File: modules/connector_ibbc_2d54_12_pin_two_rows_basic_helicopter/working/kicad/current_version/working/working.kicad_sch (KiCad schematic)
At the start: 2 parts, among them J1 hi16p, J2 hi16p

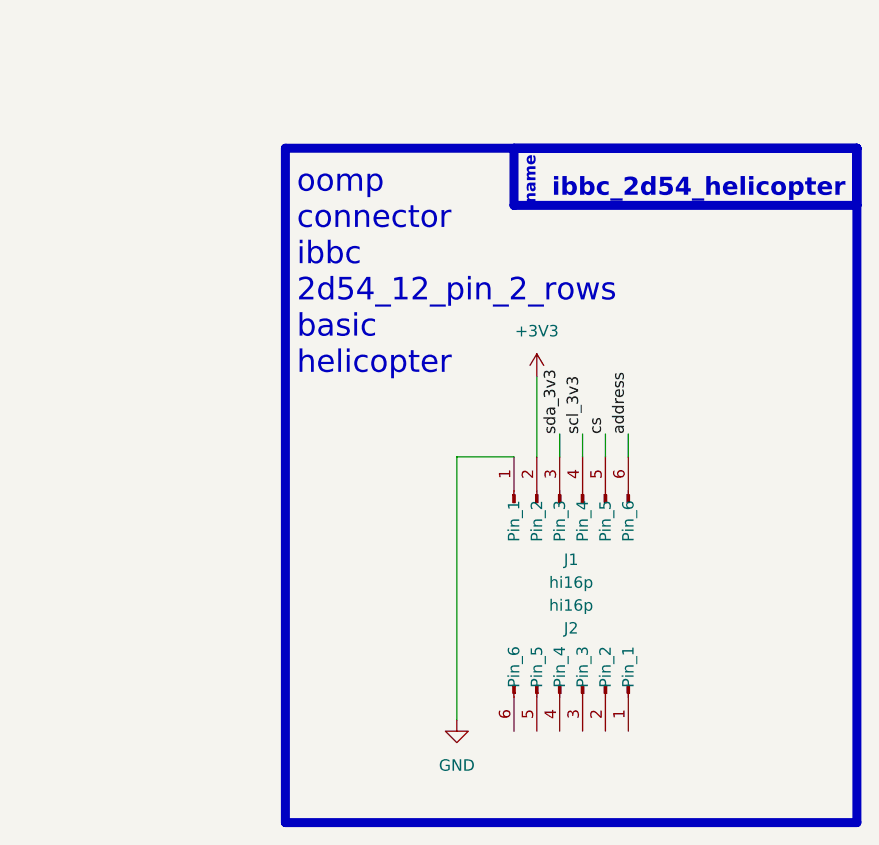
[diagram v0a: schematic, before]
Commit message: fixed formatting to be more consistent
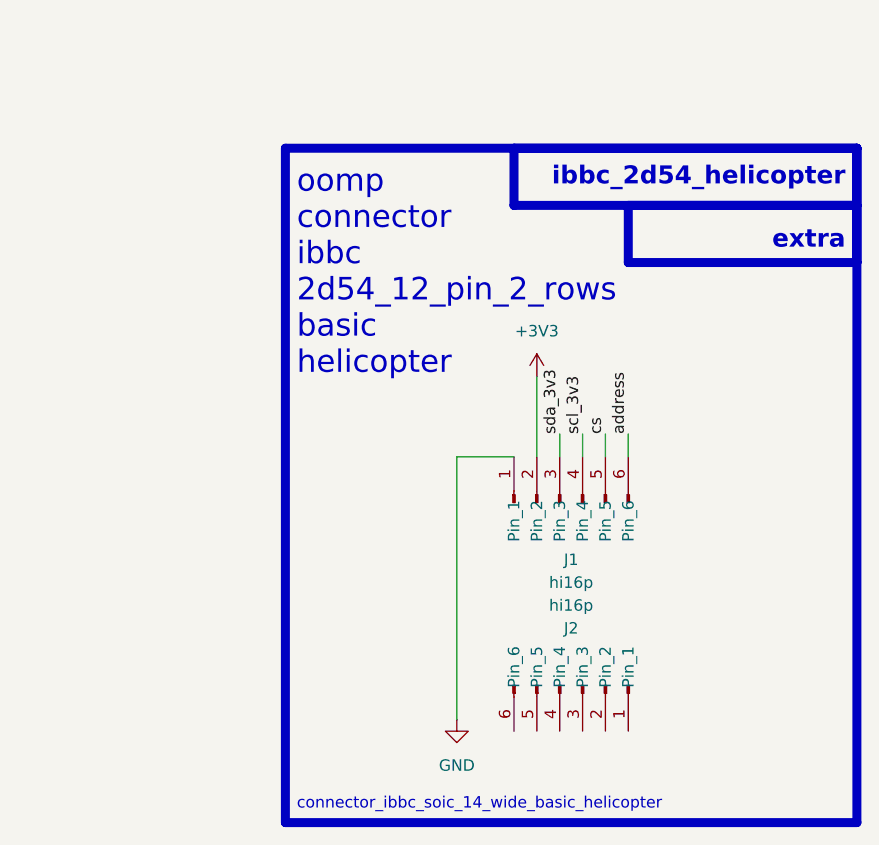
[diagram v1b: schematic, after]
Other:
- note added: "connector_ibbc_soic_14_wide_basic_helicopter"
- note added: "extra"
- note removed: "name"
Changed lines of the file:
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@@
   (rectangle (start 129.54 46.99) (end 167.64 53.34)
     (stroke (width 1) (type default))
-    (fill (type color) (color 0 0 0 0))
+    (fill (type none))
   )
-  (text "ibbc_2d54_helicopter\n	" (at 166.37 55.88 0)
-    (effects (font (size 2 2) (thickness 0.8) bold (color 255 255 255 1)) (justify right bottom))
+  (rectangle (start 142.24 53.34) (end 167.64 59.69)
+    (stroke (width 1) (type default))
+    (fill (type none))
   )
-  (text "name" (at 132.08 53.34 90)
-    (effects (font (size 1.27 1.27) (thickness 0.254) bold (color 255 255 255 1)) (justify left bottom))
+  (text "ibbc_2d54_helicopter\n	" (at 166.37 54.61 0)
+    (effects (font (size 2 2) (thickness 0.8) bold) (justify right bottom))
   )
   (text "oomp\nconnector\nibbc\n2d54_12_pin_2_rows\nbasic\nhelicopter"
@@
     (effects (font (size 2.5 2.5)) (justify left bottom))
   )
+  (text "extra" (at 166.37 58.42 0)
+    (effects (font (size 2 2) (thickness 0.8) bold) (justify right bottom))
+  )
+  (text "connector_ibbc_soic_14_wide_basic_helicopter" (at 105.41 120.65 0)
+    (effects (font (size 1.27 1.27)) (justify left bottom))
+  )
   (label "address" (at 142.24 78.74 90) (fields_autoplaced)

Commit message: schematic formatting
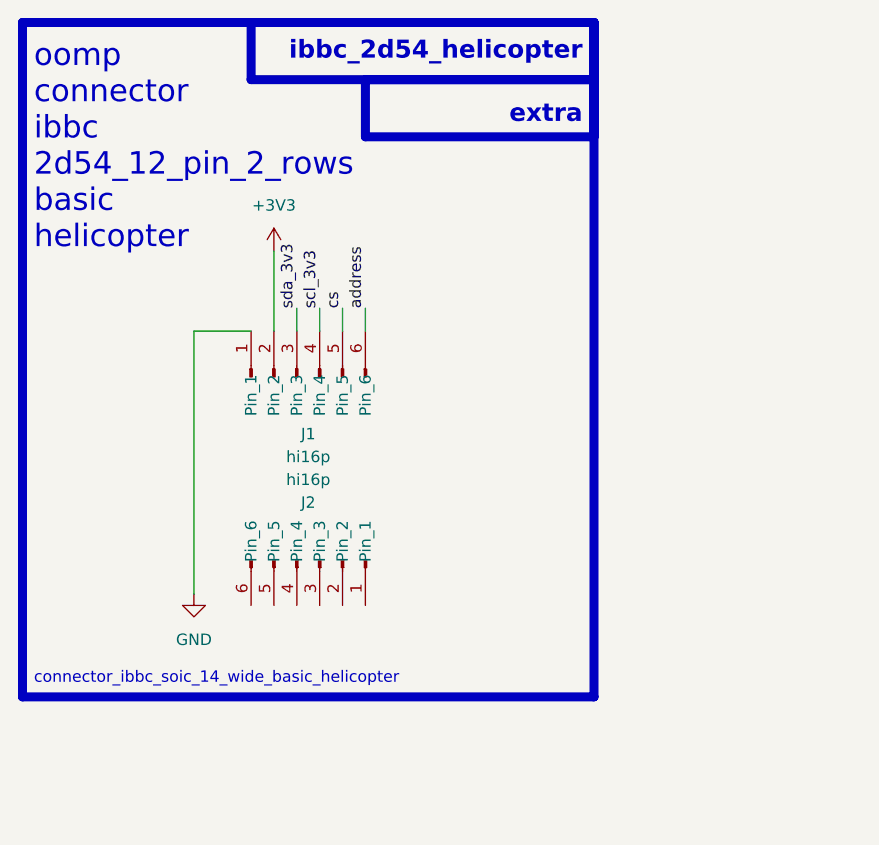
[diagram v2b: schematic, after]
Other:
- moved on the sheet: J1, J2
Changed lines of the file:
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@@
 (kicad_sch (version 20230121) (generator eeschema)
-  (paper "A4")
-  (wire (pts (xy 137.16 78.74) (xy 137.16 81.28))
+  (paper "A5")
+  (wire (pts (xy 107.95 64.77) (xy 107.95 67.31))
     (stroke (width 0) (type default))
   )
-  (wire (pts (xy 123.19 81.28) (xy 123.19 110.49))
+  (wire (pts (xy 93.98 67.31) (xy 93.98 96.52))
     (stroke (width 0) (type default))
   )
-  (wire (pts (xy 134.62 78.74) (xy 134.62 81.28))
+  (wire (pts (xy 105.41 64.77) (xy 105.41 67.31))
     (stroke (width 0) (type default))
   )
-  (wire (pts (xy 132.08 72.39) (xy 132.08 81.28))
+  (wire (pts (xy 102.87 58.42) (xy 102.87 67.31))
     (stroke (width 0) (type default))
   )
-  (wire (pts (xy 142.24 78.74) (xy 142.24 81.28))
+  (wire (pts (xy 113.03 64.77) (xy 113.03 67.31))
     (stroke (width 0) (type default))
   )
-  (wire (pts (xy 129.54 81.28) (xy 123.19 81.28))
+  (wire (pts (xy 100.33 67.31) (xy 93.98 67.31))
     (stroke (width 0) (type default))
   )
-  (wire (pts (xy 139.7 78.74) (xy 139.7 81.28))
+  (wire (pts (xy 110.49 64.77) (xy 110.49 67.31))
     (stroke (width 0) (type default))
   )
-  (rectangle (start 104.14 46.99) (end 167.64 121.92)
+  (rectangle (start 74.93 33.02) (end 138.43 107.95)
     (stroke (width 1) (type default))
     (fill (type none))
   )
-  (rectangle (start 129.54 46.99) (end 167.64 53.34)
+  (rectangle (start 100.33 33.02) (end 138.43 39.37)
     (stroke (width 1) (type default))
     (fill (type none))
   )
-  (rectangle (start 142.24 53.34) (end 167.64 59.69)
+  (rectangle (start 113.03 39.37) (end 138.43 45.72)
     (stroke (width 1) (type default))
     (fill (type none))
   )
-  (text "ibbc_2d54_helicopter\n	" (at 166.37 54.61 0)
+  (text "ibbc_2d54_helicopter\n	" (at 137.16 40.64 0)
     (effects (font (size 2 2) (thickness 0.8) bold) (justify right bottom))
   )
   (text "oomp\nconnector\nibbc\n2d54_12_pin_2_rows\nbasic\nhelicopter"
-    (at 105.41 72.39 0)
+    (at 76.2 58.42 0)
     (effects (font (size 2.5 2.5)) (justify left bottom))
   )
-  (text "extra" (at 166.37 58.42 0)
+  (text "extra" (at 137.16 44.45 0)
     (effects (font (size 2 2) (thickness 0.8) bold) (justify right bottom))
   )
-  (text "connector_ibbc_soic_14_wide_basic_helicopter" (at 105.41 120.65 0)
+  (text "connector_ibbc_soic_14_wide_basic_helicopter" (at 76.2 106.68 0)
     (effects (font (size 1.27 1.27)) (justify left bottom))
   )
-  (label "address" (at 142.24 78.74 90) (fields_autoplaced)
+  (label "address" (at 113.03 64.77 90) (fields_autoplaced)
     (effects (font (size 1.27 1.27)) (justify left bottom))
   )
-  (label "cs" (at 139.7 78.74 90) (fields_autoplaced)
+  (label "cs" (at 110.49 64.77 90) (fields_autoplaced)
     (effects (font (size 1.27 1.27)) (justify left bottom))
   )
-  (label "scl_3v3" (at 137.16 78.74 90) (fields_autoplaced)
+  (label "scl_3v3" (at 107.95 64.77 90) (fields_autoplaced)
     (effects (font (size 1.27 1.27)) (justify left bottom))
   )
-  (label "sda_3v3" (at 134.62 78.74 90) (fields_autoplaced)
+  (label "sda_3v3" (at 105.41 64.77 90) (fields_autoplaced)
     (effects (font (size 1.27 1.27)) (justify left bottom))
   )
-  (symbol (lib_id "oomlout_oomp_part_symbols:hi16p_electronic_header_2d54_mm_6_pin") (at 134.62 86.36 90) (unit 1)
+  (symbol (lib_id "oomlout_oomp_part_symbols:hi16p_electronic_header_2d54_mm_6_pin") (at 105.41 72.39 90) (unit 1)
     (in_bom yes) (on_board yes) (dnp no)
-    (property "Reference" "J1" (at 135.89 92.71 90)
+    (property "Reference" "J1" (at 106.68 78.74 90)
       (effects (font (size 1.27 1.27)))
     )
-    (property "Value" "hi16p" (at 135.89 95.25 90)
+    (property "Value" "hi16p" (at 106.68 81.28 90)
       (effects (font (size 1.27 1.27)))
     )
-    (property "Footprint" "oomlout_oomp_part_footprints:hi16p_electronic_header_2d54_mm_6_pin" (at 134.62 86.36 0)
+    (property "Footprint" "oomlout_oomp_part_footprints:hi16p_electronic_header_2d54_mm_6_pin" (at 105.41 72.39 0)
       (effects (font (size 1.27 1.27)) hide)
     )
-    (property "Datasheet" "https://github.com/oomlout/oomlout_oomp_v3/parts/electronic_header_2d54_mm_6_pin/datasheet.pdf" (at 134.62 86.36 0)
+    (property "Datasheet" "https://github.com/oomlout/oomlout_oomp_v3/parts/electronic_header_2d54_mm_6_pin/datasheet.pdf" (at 105.41 72.39 0)
       (effects (font (size 1.27 1.27)) hide)
     )
@@
     )
   )
-  (symbol (lib_id "power:GND") (at 123.19 110.49 0) (unit 1)
+  (symbol (lib_id "power:GND") (at 93.98 96.52 0) (unit 1)
     (in_bom yes) (on_board yes) (dnp no) (fields_autoplaced)
-    (property "Reference" "#PWR05" (at 123.19 116.84 0)
+    (property "Reference" "#PWR05" (at 93.98 102.87 0)
       (effects (font (size 1.27 1.27)) hide)
     )
-    (property "Value" "GND" (at 123.19 115.57 0)
+    (property "Value" "GND" (at 93.98 101.6 0)
       (effects (font (size 1.27 1.27)))
     )
-    (property "Footprint" "" (at 123.19 110.49 0)
+    (property "Footprint" "" (at 93.98 96.52 0)
       (effects (font (size 1.27 1.27)) hide)
     )
-    (property "Datasheet" "" (at 123.19 110.49 0)
+    (property "Datasheet" "" (at 93.98 96.52 0)
       (effects (font (size 1.27 1.27)) hide)
     )
@@
     )
   )
-  (symbol (lib_id "power:+3V3") (at 132.08 72.39 0) (unit 1)
+  (symbol (lib_id "power:+3V3") (at 102.87 58.42 0) (unit 1)
     (in_bom yes) (on_board yes) (dnp no) (fields_autoplaced)
-    (property "Reference" "#PWR06" (at 132.08 76.2 0)
+    (property "Reference" "#PWR06" (at 102.87 62.23 0)
       (effects (font (size 1.27 1.27)) hide)
     )
-    (property "Value" "+3V3" (at 132.08 67.31 0)
+    (property "Value" "+3V3" (at 102.87 53.34 0)
       (effects (font (size 1.27 1.27)))
     )
-    (property "Footprint" "" (at 132.08 72.39 0)
+    (property "Footprint" "" (at 102.87 58.42 0)
       (effects (font (size 1.27 1.27)) hide)
     )
-    (property "Datasheet" "" (at 132.08 72.39 0)
+    (property "Datasheet" "" (at 102.87 58.42 0)
       (effects (font (size 1.27 1.27)) hide)
     )
@@
     )
   )
-  (symbol (lib_id "oomlout_oomp_part_symbols:hi16p_electronic_header_2d54_mm_6_pin") (at 137.16 106.68 270) (unit 1)
+  (symbol (lib_id "oomlout_oomp_part_symbols:hi16p_electronic_header_2d54_mm_6_pin") (at 107.95 92.71 270) (unit 1)
     (in_bom yes) (on_board yes) (dnp no)
-    (property "Reference" "J2" (at 135.89 100.33 90)
+    (property "Reference" "J2" (at 106.68 86.36 90)
       (effects (font (size 1.27 1.27)))
     )
-    (property "Value" "hi16p" (at 135.89 97.79 90)
+    (property "Value" "hi16p" (at 106.68 83.82 90)
       (effects (font (size 1.27 1.27)))
     )
-    (property "Footprint" "oomlout_oomp_part_footprints:hi16p_electronic_header_2d54_mm_6_pin" (at 137.16 106.68 0)
+    (property "Footprint" "oomlout_oomp_part_footprints:hi16p_electronic_header_2d54_mm_6_pin" (at 107.95 92.71 0)
       (effects (font (size 1.27 1.27)) hide)
     )
-    (property "Datasheet" "https://github.com/oomlout/oomlout_oomp_v3/parts/electronic_header_2d54_mm_6_pin/datasheet.pdf" (at 137.16 106.68 0)
+    (property "Datasheet" "https://github.com/oomlout/oomlout_oomp_v3/parts/electronic_header_2d54_mm_6_pin/datasheet.pdf" (at 107.95 92.71 0)
       (effects (font (size 1.27 1.27)) hide)
     )
